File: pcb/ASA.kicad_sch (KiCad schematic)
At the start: 35 parts, among them J1 Screw_Terminal_01x02, J2 Conn_01x03_Pin, Q1 AO3400A, U1 LM386

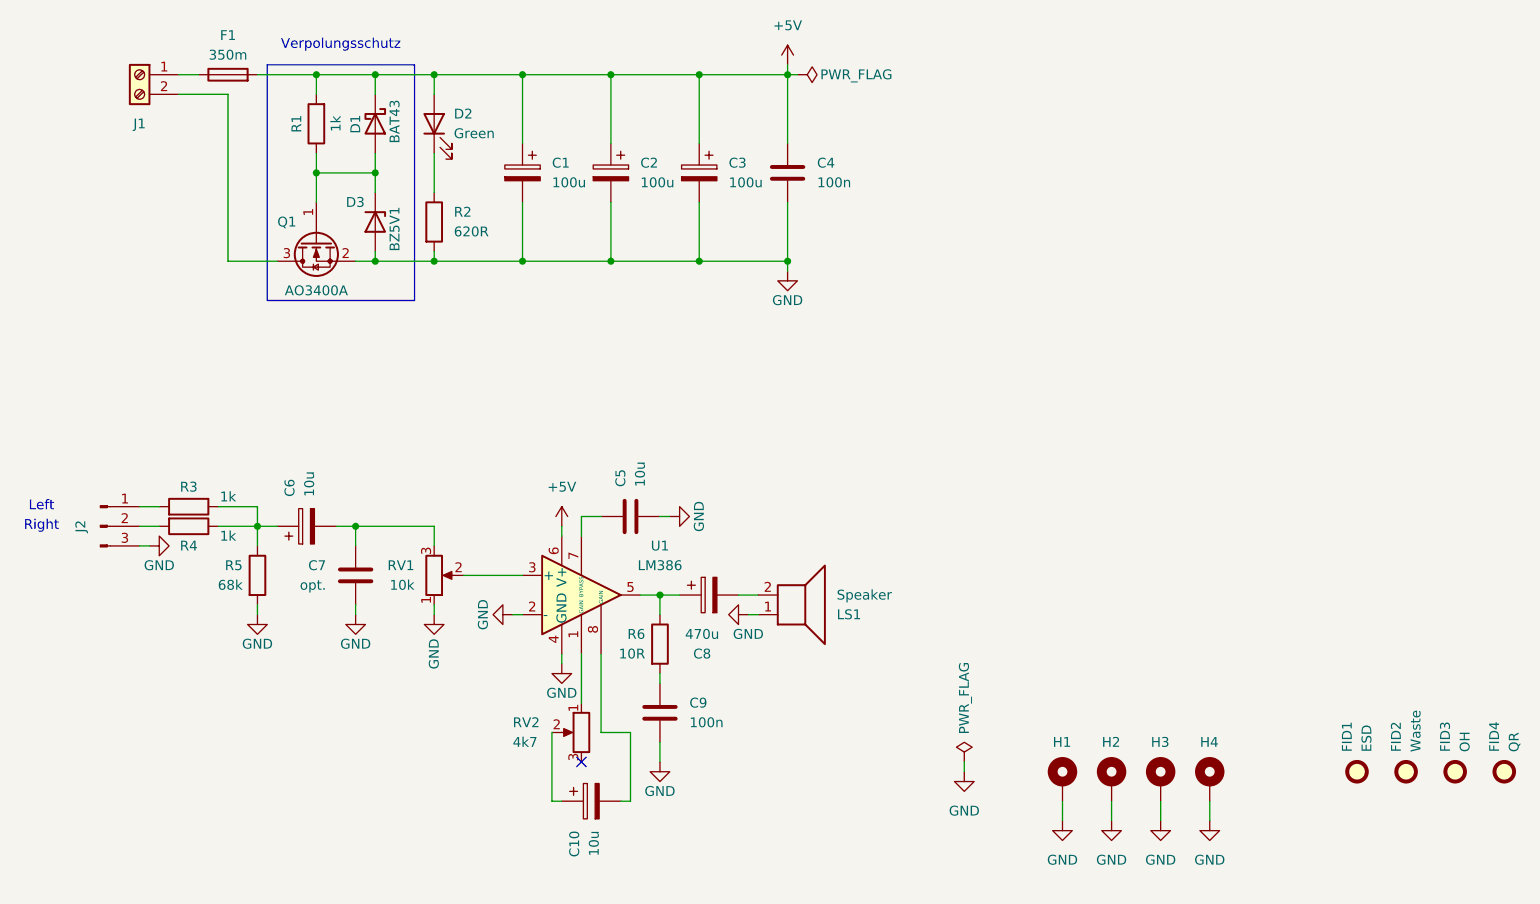
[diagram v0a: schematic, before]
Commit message: Add bass boost option
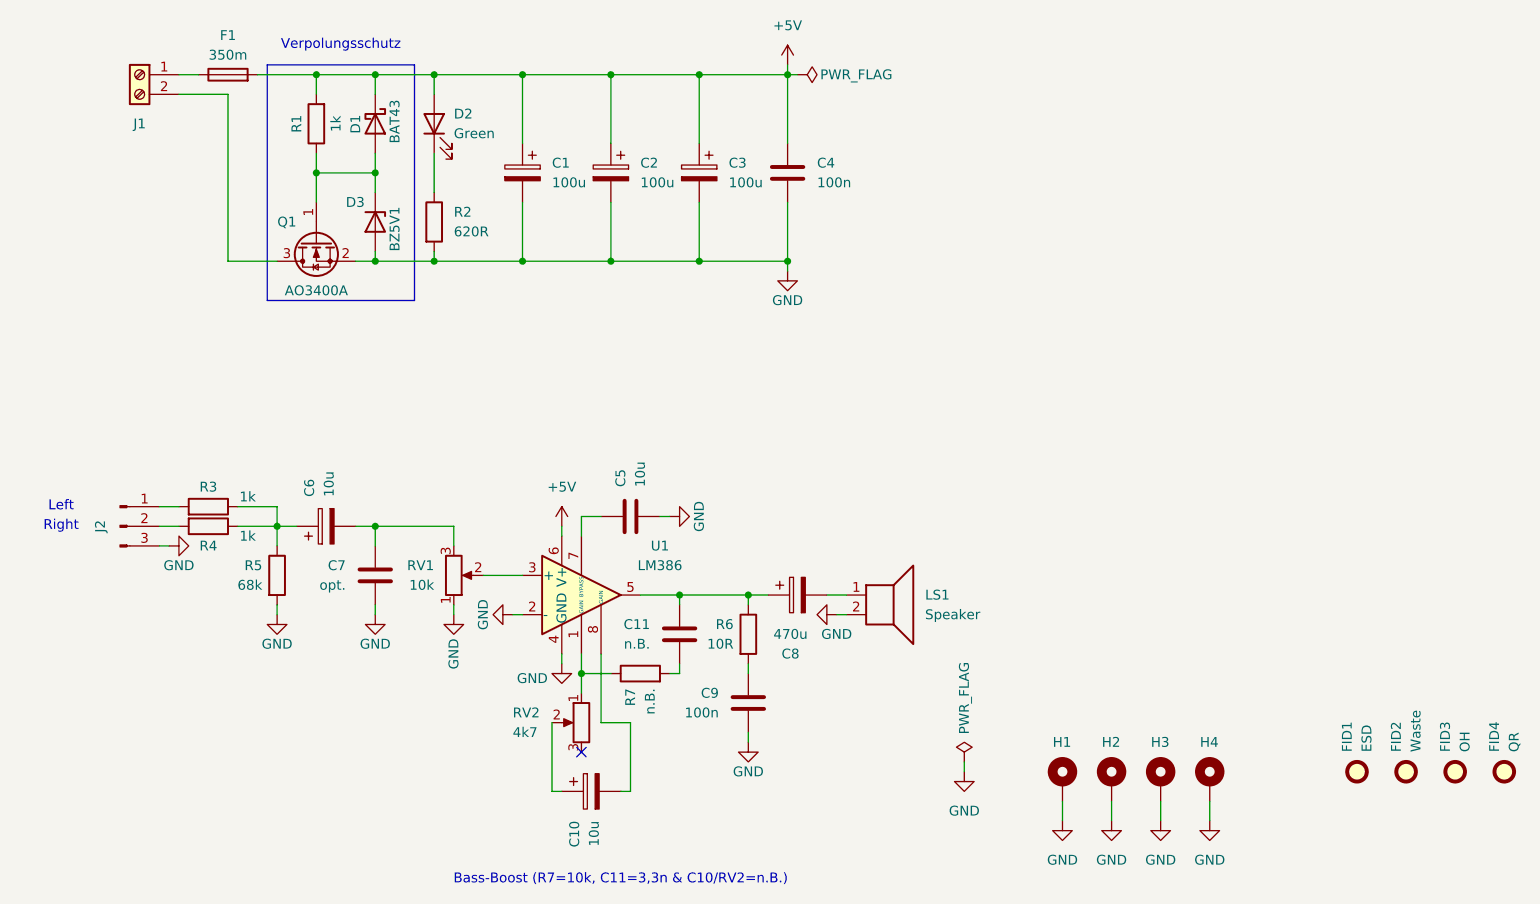
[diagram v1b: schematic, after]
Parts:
- added C11: n.B., Capacitor_SMD:C_1206_3216Metric, symbol Device:C
- added R7: n.B., Resistor_SMD:R_1206_3216Metric, symbol Device:R
- U1: HTL 100292 -> 100292, 100331
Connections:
- net GND: now also LS1.2; no longer LS1.1
- net at RV2.1, U1.1 (GAIN): now also R7.1
- net at C8.2: now also LS1.1; no longer LS1.2
- net at C8.1, R6.1, U1.5: now also C11.1
- new net: C11.2, R7.2
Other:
- note added: "Bass-Boost (R7=10k, C11=3,3n & C10/RV2=n.B.)"
- moved on the sheet: C10, C6, C7, C8, C9, J2, LS1, R3, R4, R5, R6, RV1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
